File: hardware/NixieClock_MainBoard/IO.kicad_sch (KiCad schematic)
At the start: 9 parts, among them J8 Conn_01x08, J9 Conn_01x03, U13 NC7SZ125M5X, U6 PCA9583A

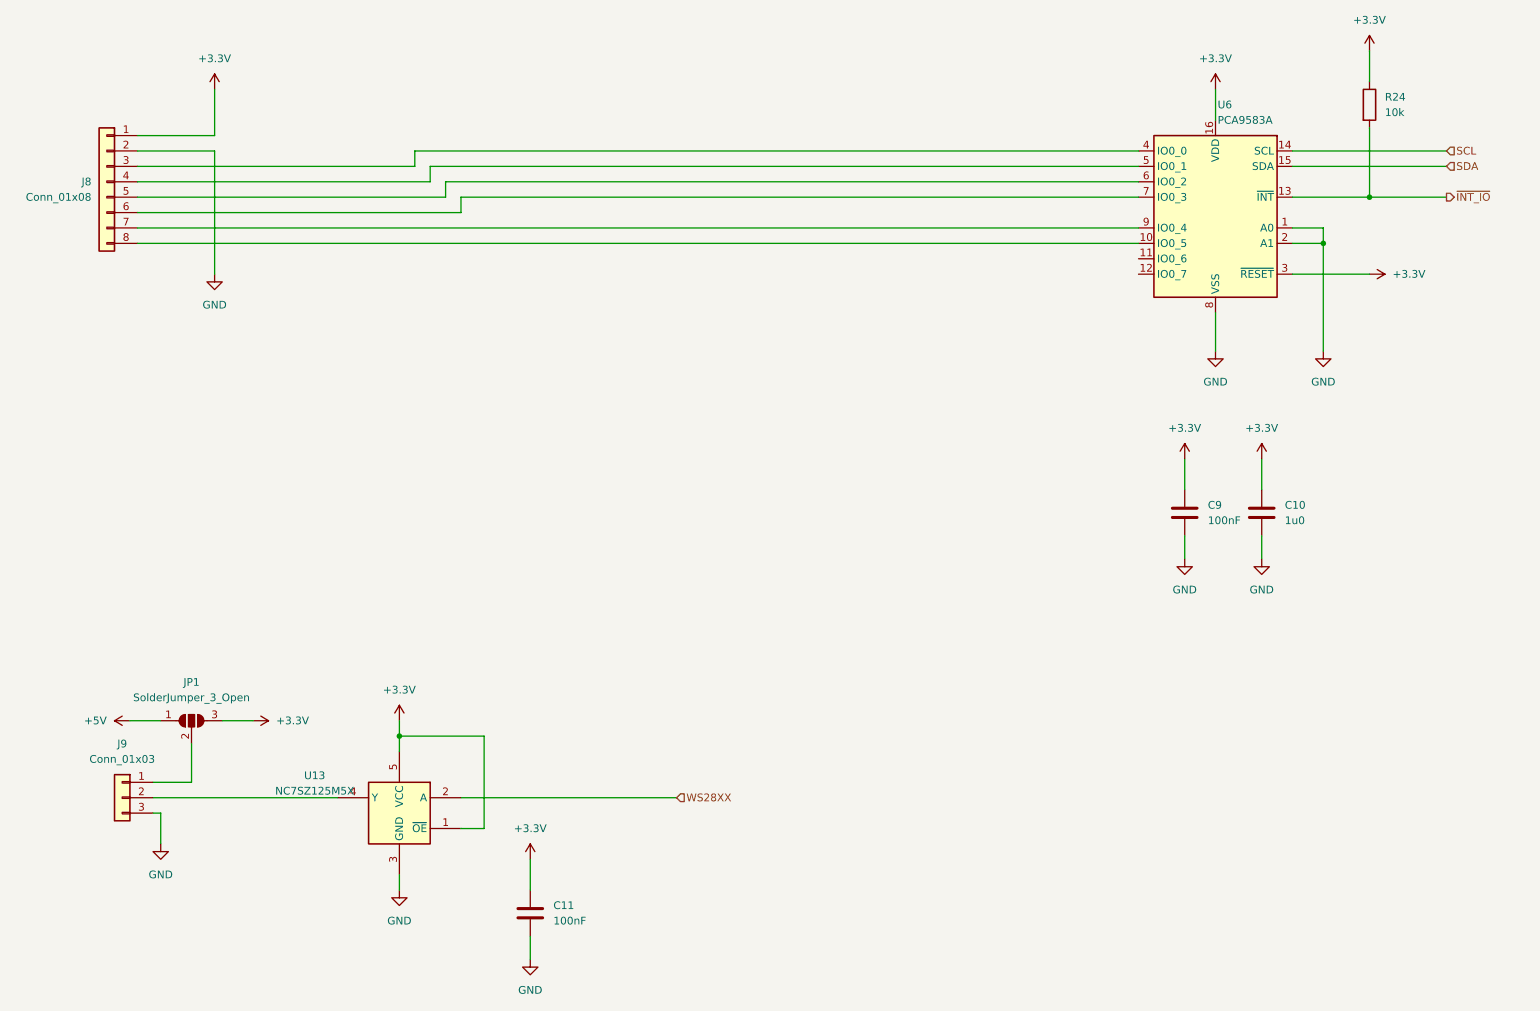
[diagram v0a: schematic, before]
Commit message: change sd card footprint changes on mainboard layout add stl files for display case
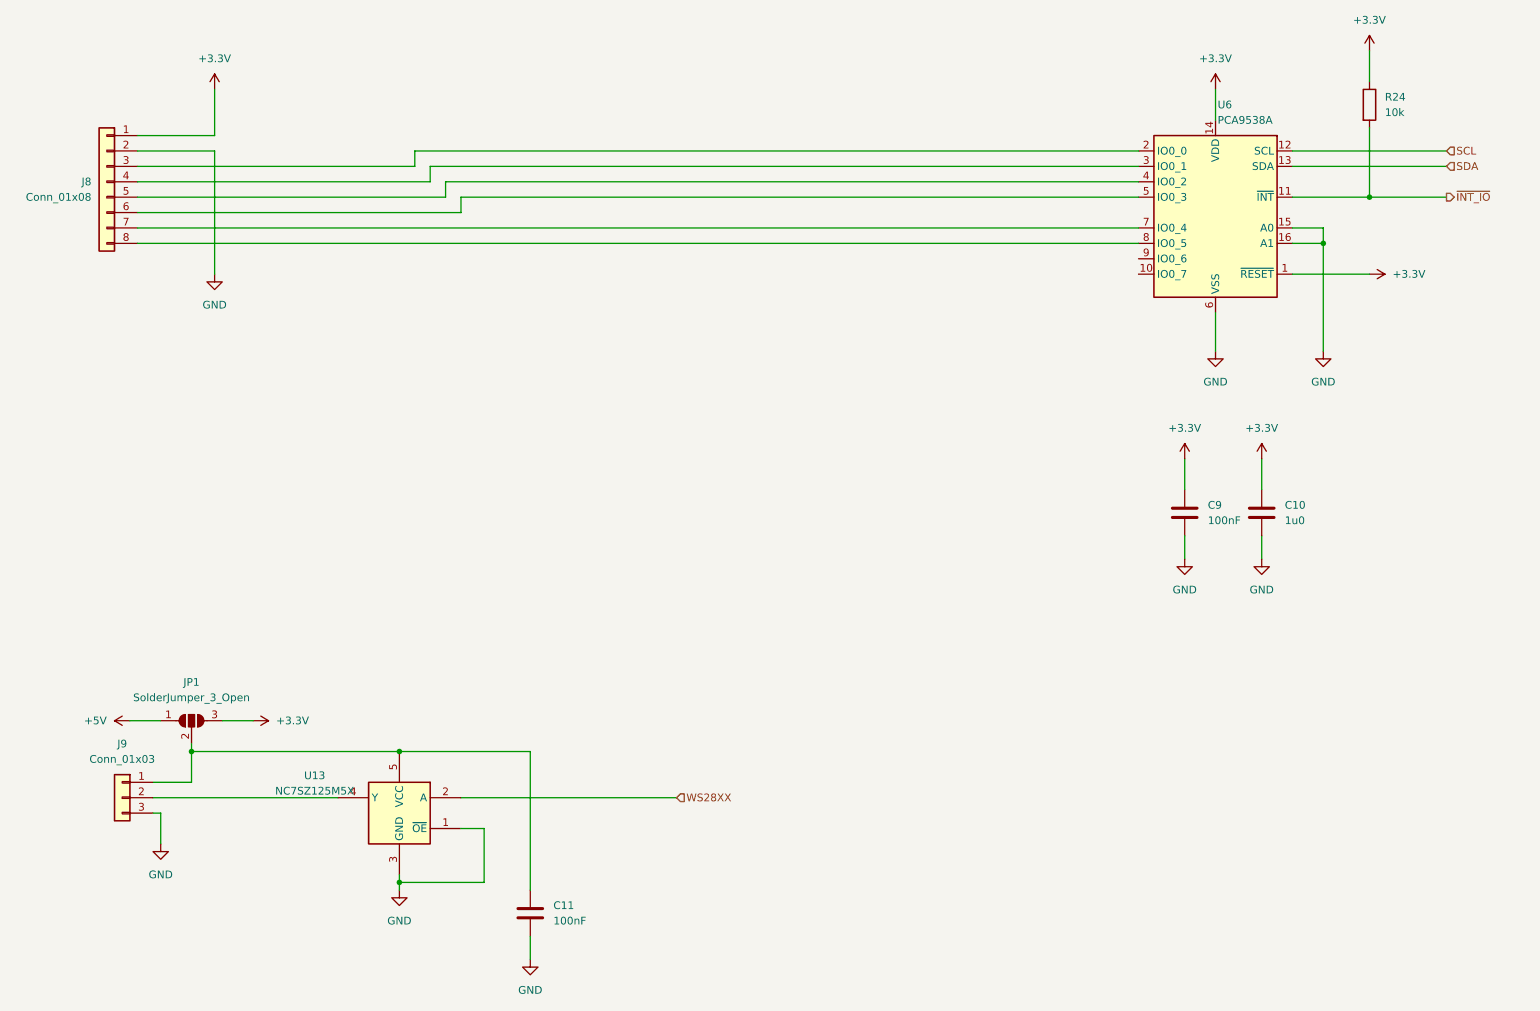
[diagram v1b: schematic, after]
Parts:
- U6: value PCA9583A -> PCA9538A
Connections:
- net +3.3V: now also U6.1 (~{RESET}), U6.14 (VDD); no longer C11.1, U13.1 (~{OE}), U13.5 (VCC), U6.16 (VDD), U6.3 (~{RESET})
- net GND: now also U13.1 (~{OE}), U6.15 (A0), U6.16 (A1), U6.6 (VSS); no longer U6.1 (A0), U6.2 (A1), U6.8 (VSS)
- net SCL: now also U6.12 (SCL); no longer U6.14 (SCL)
- net SDA: now also U6.13 (SDA); no longer U6.15 (SDA)
- net ~{INT_IO}: now also U6.11 (~{INT}); no longer U6.13 (~{INT})
- net at J9.1 (Pin_1), JP1.2 (C): now also C11.1, U13.5 (VCC)
- net at U6.10 (IO0_7): no longer J8.8 (Pin_8)
- net at J8.3 (Pin_3): now also U6.2 (IO0_0); no longer U6.4 (IO0_0)
- net at J8.4 (Pin_4): now also U6.3 (IO0_1); no longer U6.5 (IO0_1)
- net at J8.5 (Pin_5): now also U6.4 (IO0_2); no longer U6.6 (IO0_2)
- net at J8.6 (Pin_6): now also U6.5 (IO0_3); no longer U6.7 (IO0_3)
- net at J8.7 (Pin_7): now also U6.7 (IO0_4); no longer U6.9 (IO0_4)
- new net: J8.8 (Pin_8), U6.8 (IO0_5)
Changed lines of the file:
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@@
 	(paper "A4")
 	(junction
-		(at 81.28 134.62)
+		(at 46.99 137.16)
+		(diameter 0)
+		(color 0 0 0 0)
+	)
+	(junction
+		(at 81.28 158.75)
 		(diameter 0)
 		(color 0 0 0 0)
@@
 	)
 	(junction
+		(at 81.28 137.16)
+		(diameter 0)
+		(color 0 0 0 0)
+	)
+	(junction
 		(at 233.68 53.34)
 		(diameter 0)
@@
 	(wire
 		(pts
-			(xy 102.87 154.94) (xy 102.87 160.02)
+			(xy 102.87 137.16) (xy 102.87 160.02)
 		)
 		(stroke
@@
 	(wire
 		(pts
-			(xy 81.28 134.62) (xy 81.28 137.16)
-		)
-		(stroke
-			(width 0)
-			(type default)
-		)
-	)
-	(wire
-		(pts
 			(xy 228.6 38.1) (xy 254 38.1)
 		)
@@
 	(wire
 		(pts
+			(xy 81.28 158.75) (xy 81.28 160.02)
+		)
+		(stroke
+			(width 0)
+			(type default)
+		)
+	)
+	(wire
+		(pts
 			(xy 41.91 152.4) (xy 41.91 147.32)
 		)
@@
 	(wire
 		(pts
-			(xy 81.28 132.08) (xy 81.28 134.62)
-		)
-		(stroke
-			(width 0)
-			(type default)
-		)
-	)
-	(wire
-		(pts
 			(xy 210.82 88.9) (xy 210.82 93.98)
 		)
@@
 	(wire
 		(pts
+			(xy 95.25 149.86) (xy 95.25 158.75)
+		)
+		(stroke
+			(width 0)
+			(type default)
+		)
+	)
+	(wire
+		(pts
 			(xy 88.9 45.72) (xy 88.9 43.18)
 		)
@@
 	(wire
 		(pts
+			(xy 46.99 137.16) (xy 46.99 142.24)
+		)
+		(stroke
+			(width 0)
+			(type default)
+		)
+	)
+	(wire
+		(pts
 			(xy 203.2 40.64) (xy 86.36 40.64)
 		)
@@
 	(wire
 		(pts
+			(xy 102.87 137.16) (xy 81.28 137.16)
+		)
+		(stroke
+			(width 0)
+			(type default)
+		)
+	)
+	(wire
+		(pts
 			(xy 223.52 88.9) (xy 223.52 93.98)
 		)
@@
 	(wire
 		(pts
+			(xy 95.25 158.75) (xy 81.28 158.75)
+		)
+		(stroke
+			(width 0)
+			(type default)
+		)
+	)
+	(wire
+		(pts
 			(xy 36.83 132.08) (xy 41.91 132.08)
 		)
@@
 	(wire
 		(pts
-			(xy 95.25 149.86) (xy 95.25 134.62)
-		)
-		(stroke
-			(width 0)
-			(type default)
-		)
-	)
-	(wire
-		(pts
 			(xy 50.8 38.1) (xy 50.8 58.42)
 		)
@@
 	(wire
 		(pts
-			(xy 46.99 135.89) (xy 46.99 142.24)
-		)
-		(stroke
-			(width 0)
-			(type default)
-		)
-	)
-	(wire
-		(pts
-			(xy 81.28 157.48) (xy 81.28 160.02)
+			(xy 46.99 135.89) (xy 46.99 137.16)
+		)
+		(stroke
+			(width 0)
+			(type default)
+		)
+	)
+	(wire
+		(pts
+			(xy 81.28 157.48) (xy 81.28 158.75)
 		)
 		(stroke
@@
 	(wire
 		(pts
+			(xy 46.99 137.16) (xy 81.28 137.16)
+		)
+		(stroke
+			(width 0)
+			(type default)
+		)
+	)
+	(wire
+		(pts
 			(xy 210.82 101.6) (xy 210.82 105.41)
-		)
-		(stroke
-			(width 0)
-			(type default)
-		)
-	)
-	(wire
-		(pts
-			(xy 95.25 134.62) (xy 81.28 134.62)
 		)
 		(stroke
@@
 			)
 		)
-		(property "Value" "PCA9583A"
+		(property "Value" "PCA9538A"
 			(at 216.2459 33.02 0)
 			(effects
@@
 				(path "/5ddb5910-d1ea-4e23-971a-19156fc3bbe9/079c23e2-2395-4de4-8770-a54833c4570a"
 					(reference "U6")
-					(unit 1)
-				)
-			)
-		)
-	)
-	(symbol
-		(lib_id "power:+3.3V")
-		(at 81.28 132.08 0)
-		(unit 1)
-		(exclude_from_sim no)
-		(in_bom yes)
-		(on_board yes)
-		(dnp no)
-		(fields_autoplaced yes)
-		(property "Reference" "#PWR054"
-			(at 81.28 135.89 0)
-			(effects
-				(font
-					(size 1.27 1.27)
-				)
-				(hide yes)
-			)
-		)
-		(property "Value" "+3.3V"
-			(at 81.28 127 0)
-			(effects
-				(font
-					(size 1.27 1.27)
-				)
-			)
-		)
-		(property "Footprint" ""
-			(at 81.28 132.08 0)
-			(effects
-				(font
-					(size 1.27 1.27)
-				)
-				(hide yes)
-			)
-		)
-		(property "Datasheet" ""
-			(at 81.28 132.08 0)
-			(effects
-				(font
-					(size 1.27 1.27)
-				)
-				(hide yes)
-			)
-		)
-		(property "Description" "Power symbol creates a global label with name \"+3.3V\""
-			(at 81.28 132.08 0)
-			(effects
-				(font
-					(size 1.27 1.27)
-				)
-				(hide yes)
-			)
-		)
-		(pin "1"
-		)
-		(instances
-			(project "NixieClock_MainBoard"
-				(path "/5ddb5910-d1ea-4e23-971a-19156fc3bbe9/079c23e2-2395-4de4-8770-a54833c4570a"
-					(reference "#PWR054")
 					(unit 1)
 				)
@@
 					(unit 1)
 				)
-			)
-		)
-	)
-	(symbol
-		(lib_id "power:+3.3V")
-		(at 102.87 154.94 0)
-		(unit 1)
-		(exclude_from_sim no)
-		(in_bom yes)
-		(on_board yes)
-		(dnp no)
-		(fields_autoplaced yes)
-		(property "Reference" "#PWR052"
-			(at 102.87 158.75 0)
-			(effects
-				(font
-					(size 1.27 1.27)
-				)
-				(hide yes)
-			)
-		)
-		(property "Value" "+3.3V"
-			(at 102.87 149.86 0)
-			(effects
-				(font
-					(size 1.27 1.27)
-				)
-			)
-		)
-		(property "Footprint" ""
-			(at 102.87 154.94 0)
-			(effects
-				(font
-					(size 1.27 1.27)
-				)
-				(hide yes)
-			)
-		)
-		(property "Datasheet" ""
-			(at 102.87 154.94 0)
-			(effects
-				(font
-					(size 1.27 1.27)
-				)
-				(hide yes)
-			)
-		)
-		(property "Description" "Power symbol creates a global label with name \"+3.3V\""
-			(at 102.87 154.94 0)
-			(effects
-				(font
-					(size 1.27 1.27)
-				)
-				(hide yes)
-			)
-		)
-		(pin "1"
-		)
-		(instances
-			(project "NixieClock_MainBoard"
-				(path "/5ddb5910-d1ea-4e23-971a-19156fc3bbe9/079c23e2-2395-4de4-8770-a54833c4570a"
-					(reference "#PWR052")
-					(unit 1)
-				)

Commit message: Hardware V2.1 add NixieClock_MainBoard/NixieClock_Schematic.pdf
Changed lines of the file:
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@@
 (kicad_sch
-	(version 20231120)
+	(version 20250114)
 	(generator "eeschema")
-	(generator_version "8.0")
+	(generator_version "9.0")
 	(paper "A4")
+	(title_block
+		(date "2026-06-07")
+		(rev "2.1")
+	)
 	(junction
 		(at 46.99 137.16)
@@
 		(shape input)
 		(at 254 38.1 0)
-		(fields_autoplaced yes)
 		(effects
 			(font
@@
 		(shape input)
 		(at 127 144.78 0)
-		(fields_autoplaced yes)
 		(effects
 			(font
@@
 		(shape output)
 		(at 254 45.72 0)
-		(fields_autoplaced yes)
 		(effects
 			(font
@@
 		(shape input)
 		(at 254 40.64 0)
-		(fields_autoplaced yes)
 		(effects
 			(font
